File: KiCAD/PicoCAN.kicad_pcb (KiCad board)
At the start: 2 copper layers, 21 x 51.5 mm, 52 parts, among them J1 USB_C_Receptacle_USB2.0_14P, J2 Conn_01x20, J3 Conn_01x20, J4 Conn_01x02, J5 Screw_Terminal_01x03 (C381777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, J7 Conn_01x02, SW1 SW_Push, U1 RP2040, U2 MCP1700x-330xxTT, U3 W25Q16JVUXIQ, U4 MCP25625-x-SS (C481365), Y1 12 MHz Crystal_GND24 (C9002), Y2 16 MHz Crystal_GND24 (C13738)

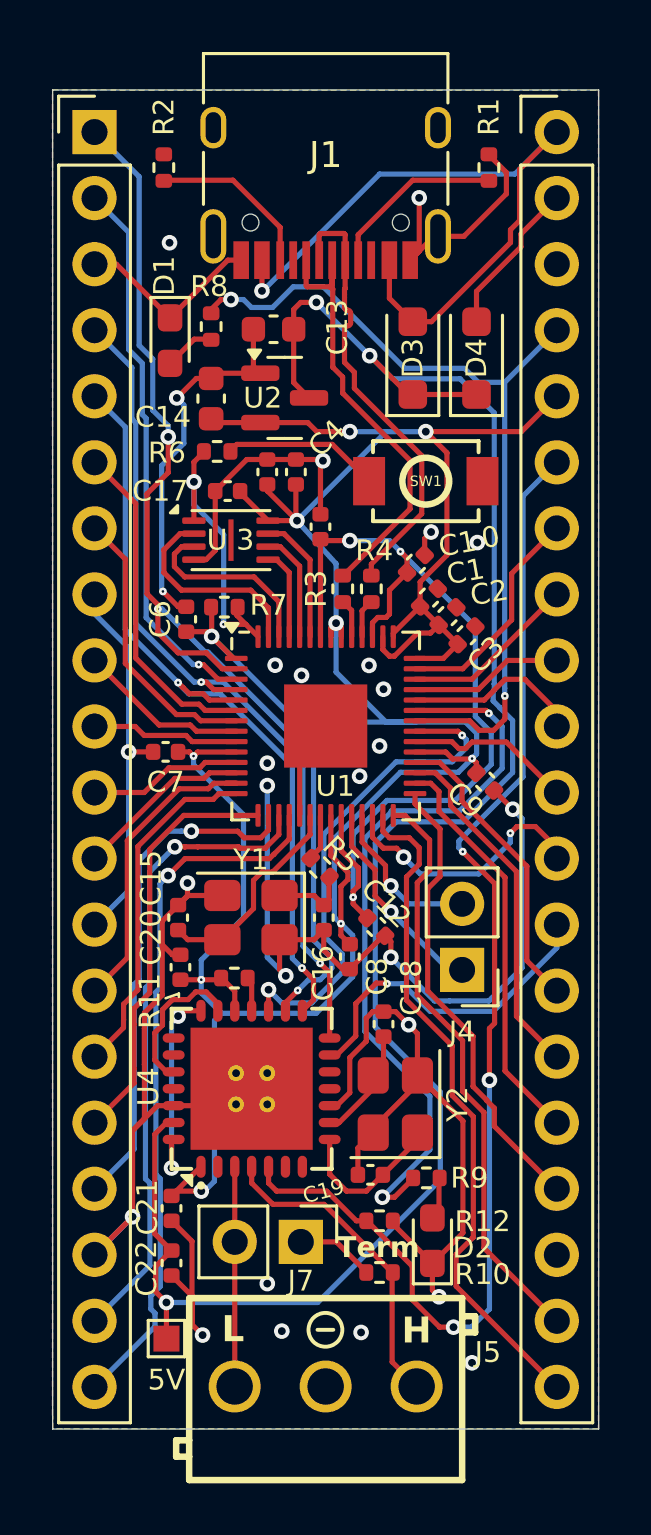
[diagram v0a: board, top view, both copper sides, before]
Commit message: MCP25625 issue fixed by rewire
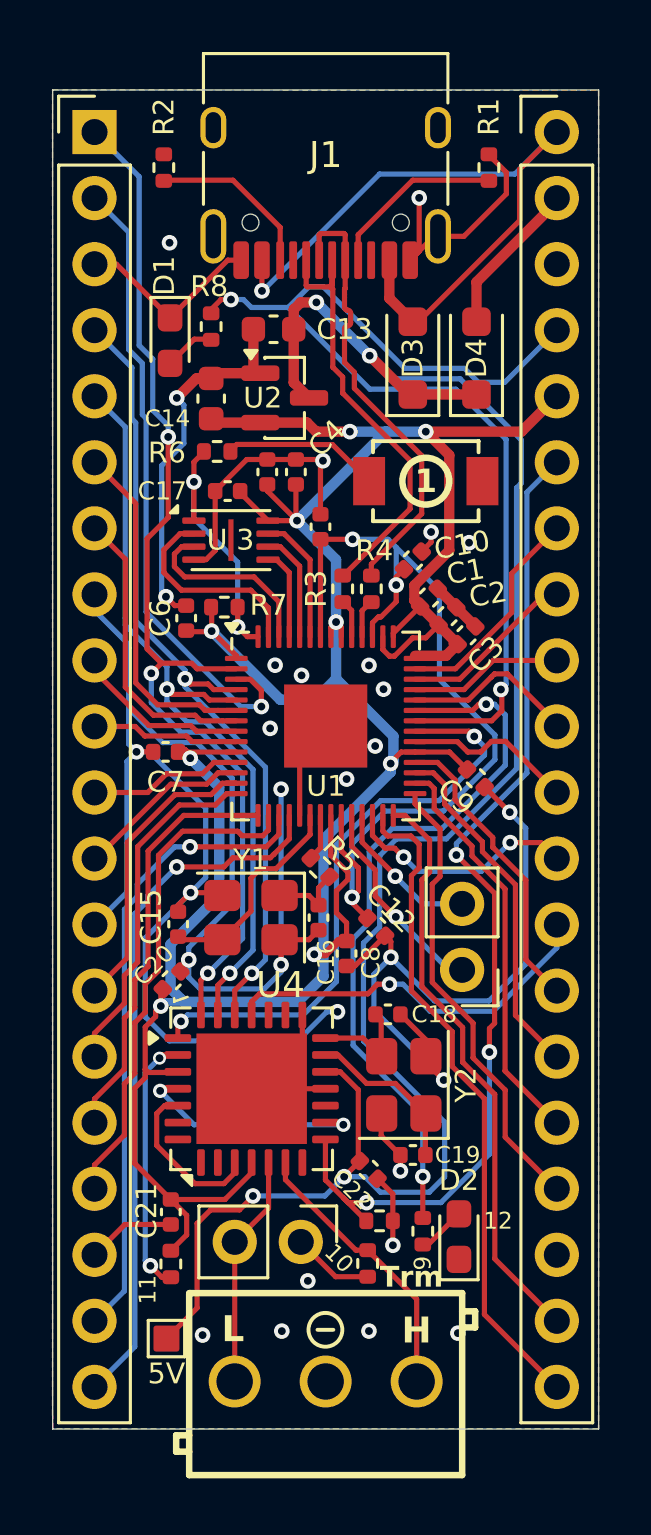
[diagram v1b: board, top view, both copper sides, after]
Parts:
- D1: value C19171390 -> C2286
- R3, R4: value 27 -> 27R
- U4: value MCP25625-x-SS (C481365) -> MCP25625x-x-ML; footprint easyeda2kicad:QFN-28_L6.0-W6.0-P0.65-BL-EP -> Package_DFN_QFN:QFN-28-1EP_6x6mm_P0.65mm_EP4.25x4.25mm
- moved R11 11.3 mm to (147.4, 116.3), turned to 90 degrees
- moved C22 8.39 mm to (155.0, 112.7), turned to -45 degrees
- moved R9 2.05 mm to (157.1, 115.1), turned to -90 degrees
- moved C19 1.80 mm to (156.7, 112.2)
- moved D2 1.03 mm to (158.5, 115.3)
- moved Y2 0.81 mm to (156.4, 109.5)
- moved C20 0.61 mm to (147.4, 105.4), turned to 45 degrees
- moved R10 0.57 mm to (155.0, 116.3), turned to 90 degrees
- moved C18 0.41 mm to (155.8, 106.7), turned to 0 degrees
- moved C9 0.38 mm to (159.2, 97.7)
- moved C15 0.25 mm to (147.7, 103.3)
- moved C16 0.20 mm to (153.1, 103.0)
- moved J5 0.19 mm to (153.4, 120.9)
- moved C8 0.17 mm to (154.2, 104.4)
- moved C10 0.17 mm to (156.7, 89.3)
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- renumbered 5V to TP1
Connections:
- U4 pad : GND -> (no net)
- U4 pad 1: +3V3 -> GPIO23
- U4 pad 10: GND -> Net-(U4-R_{XD})
- U4 pad 11: unconnected-(U4-~{Rx1BF}-Pad11) -> +3V3
- U4 pad 12: unconnected-(U4-~{Rx0BF}-Pad12) -> CANL
- U4 pad 13: INT -> CANH
- U4 pad 14: GPIO2 -> unconnected-(U4-NC-Pad14)
- U4 pad 15: GPIO3 -> STBY
- U4 pad 16: GPIO0 -> Net-(U4-T_{XD})
- U4 pad 17: GPIO23 -> unconnected-(U4-NC-Pad17)
- U4 pad 18: Net-(U4-~{RESET}) -> GND
- U4 pad 19: +3V3 -> +5V
- U4 pad 2: unconnected-(U4-NC-Pad2) -> Net-(U4-~{RESET})
- U4 pad 20: Net-(U4-TXD) -> OSC2
- U4 pad 21: Net-(U4-RXD) -> OSC1
- U4 pad 22: unconnected-(U4-CLKOUT-Pad22) -> GND
- U4 pad 24: Net-(U4-TXD) -> unconnected-(U4-~{Rx0BF}-Pad24)
- U4 pad 25: unconnected-(U4-NC-Pad25) -> INT
- U4 pad 26: GND -> GPIO2
- U4 pad 27: +5V -> GPIO3
- U4 pad 28: Net-(U4-RXD) -> GPIO0
- U4 pad 3: CANL -> +3V3
- U4 pad 4: CANH -> Net-(U4-T_{XD})
- U4 pad 5: STBY -> Net-(U4-R_{XD})
- U4 pad 8: OSC2 -> unconnected-(U4-~{Tx1RTS}-Pad8)
- U4 pad 9: OSC1 -> unconnected-(U4-~{Tx2RTS}-Pad9)
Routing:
- net Net-(U4-T_{XD}): track 0.00 -> 9.21 mm, vias 0 -> 2
- net Net-(U4-~{RESET}): track 1.33 -> 10.0 mm, vias 0 -> 2
- net STBY: track 47.2 -> 39.1 mm
- net GND: track 148.8 -> 156.9 mm, vias 28 -> 30
- net Net-(U4-RXD): track 8.04 -> 0.00 mm, vias 2 -> 0
- net GPIO24: track 33.2 -> 40.9 mm
- net Net-(U4-R_{XD}): track 0.00 -> 6.34 mm
- net Net-(U4-TXD): track 5.85 -> 0.00 mm
- net GPIO23: track 19.2 -> 22.9 mm
- net GPIO1: track 21.4 -> 24.4 mm
- net GPIO0: track 43.9 -> 41.4 mm
- net INT: track 13.0 -> 14.9 mm
- net +3V3: track 122.3 -> 120.5 mm, vias 10 -> 9
- net CANH: track 12.2 -> 10.8 mm
- net GPIO2: track 33.1 -> 31.7 mm
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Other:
- board text added: "C10"
- board text added: "SCK"
- board text added: "SI"
- board text added: "SO"
- board text added: "Trm"
- board text removed: "C1"
- board text removed: "Term"

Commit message: Swap R6 and R7
Fixes issue of button not activating BOOTSEL mode
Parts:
- moved R6 5.99 mm to (149.5, 91.1), turned to 0 degrees
- moved R7 5.99 mm to (149.2, 85.1), turned to 180 degrees
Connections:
- J1 pad SH: GND -> (no net)
- R6 pad 1: Net-(R6-Pad1) -> +3V3
- R7 pad 1: +3V3 -> Net-(R7-Pad1)
- SW1 pad 2: Net-(R6-Pad1) -> Net-(R7-Pad1)
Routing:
- net Net-(R7-Pad1): track 0.00 -> 6.06 mm
- net Net-(R6-Pad1): track 6.06 -> 0.00 mm
